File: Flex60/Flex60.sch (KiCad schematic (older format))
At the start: 6 parts

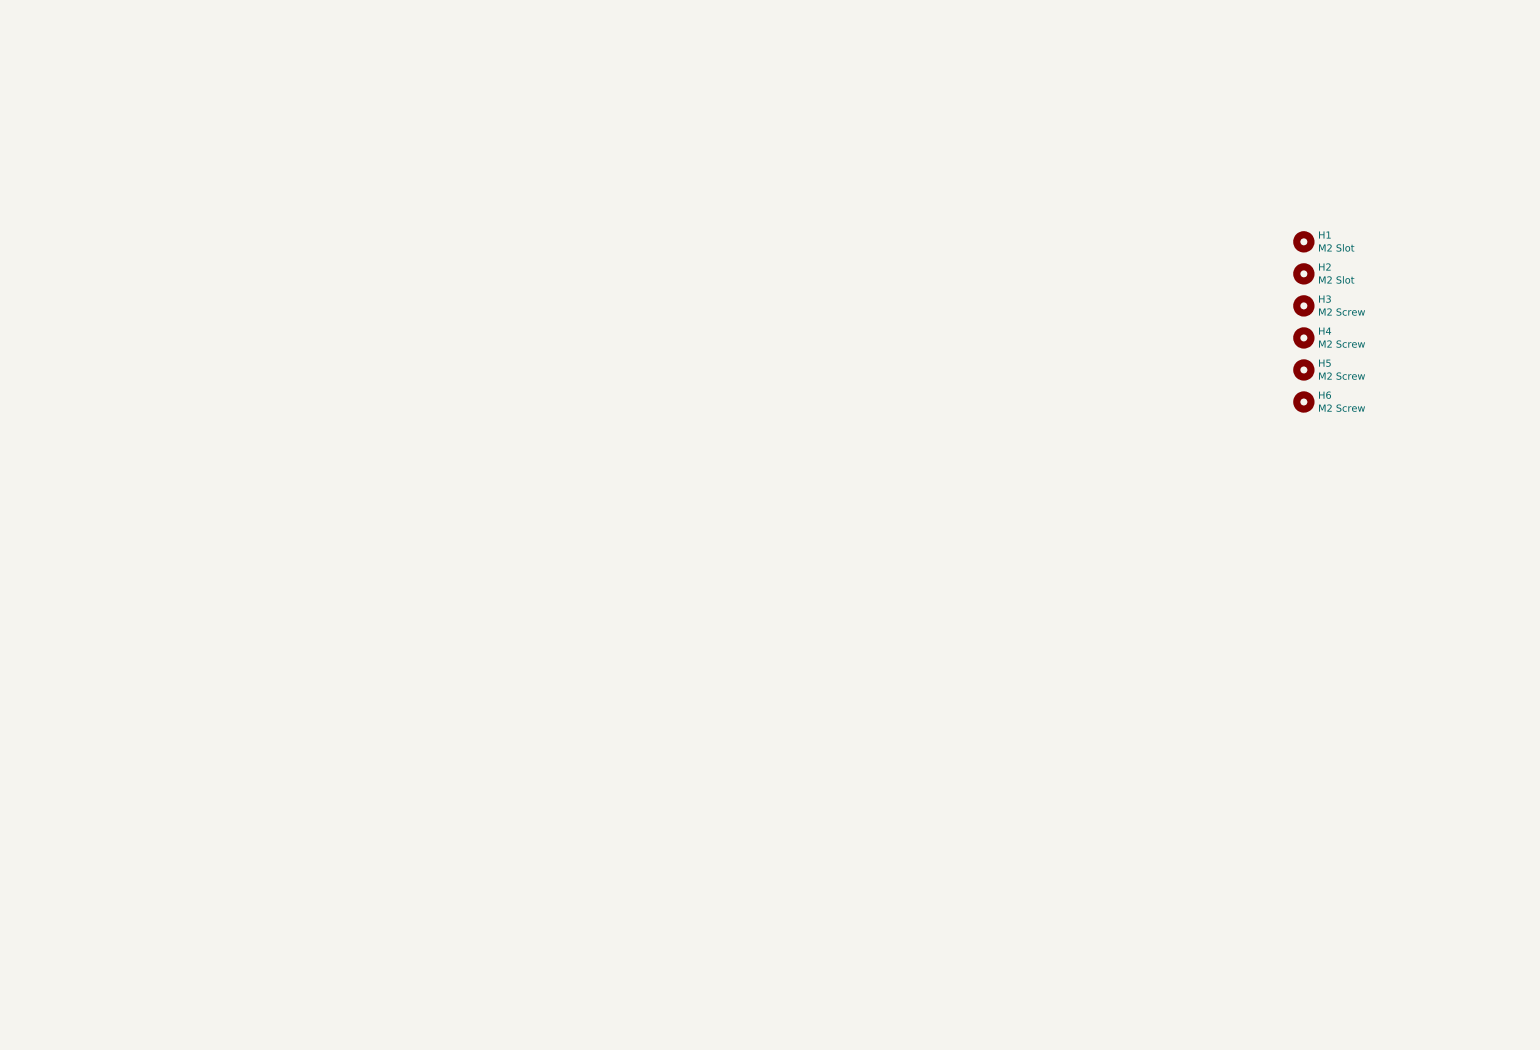
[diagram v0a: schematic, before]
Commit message: Layout of switches
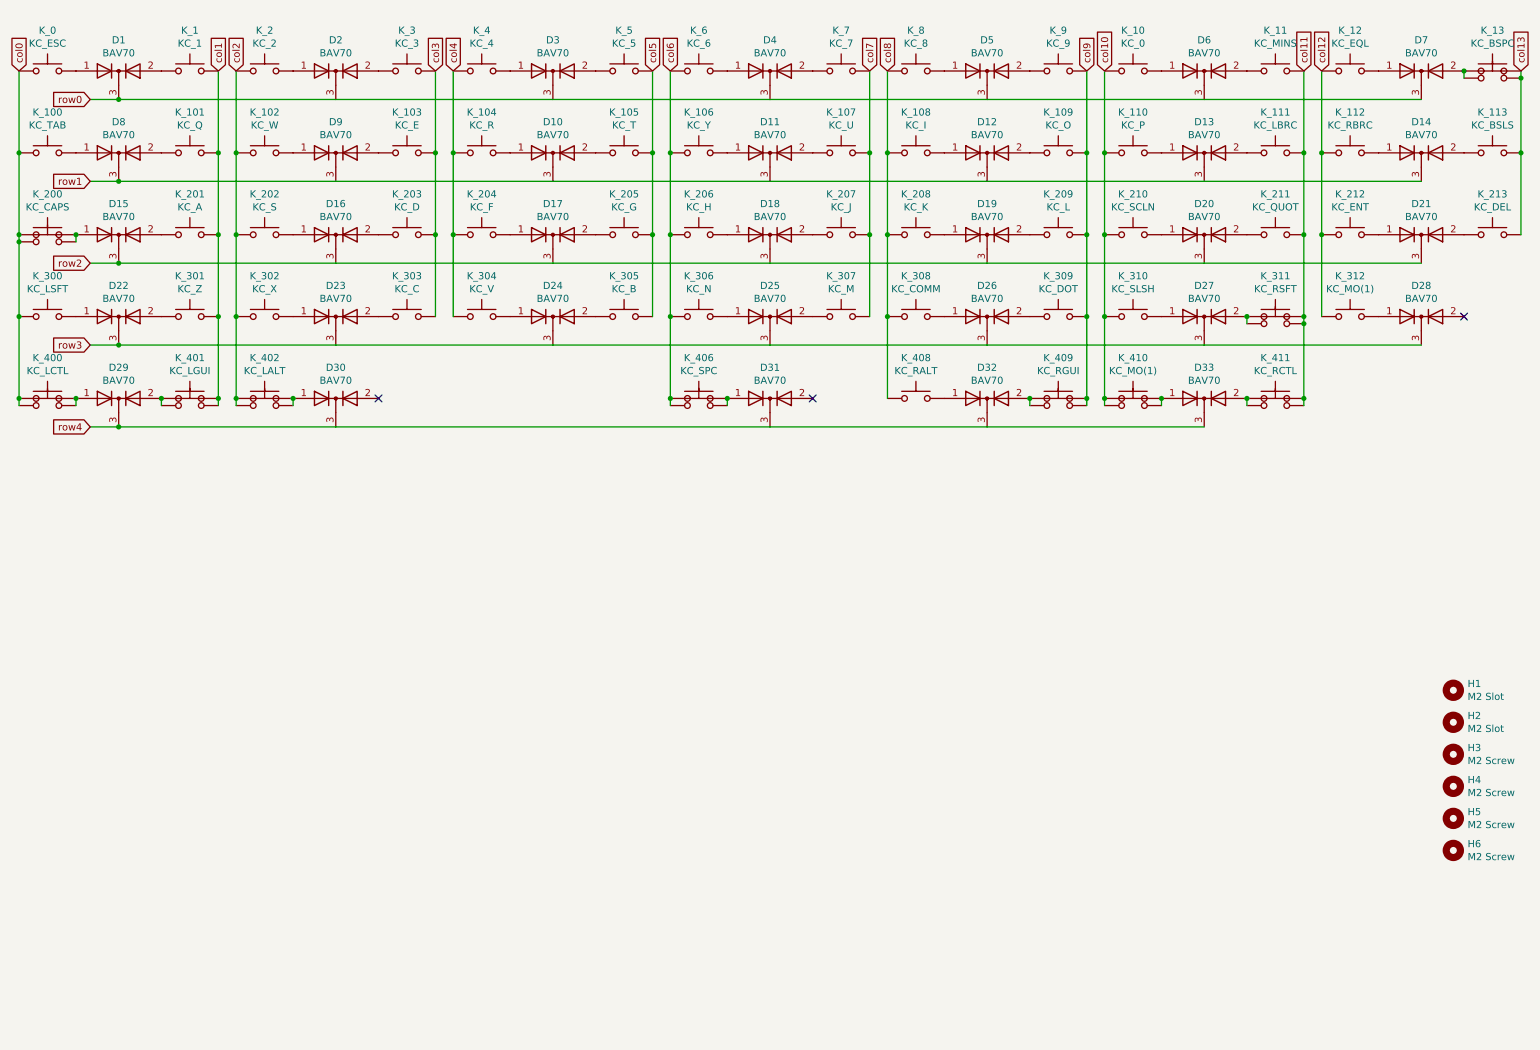
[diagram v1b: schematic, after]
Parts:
- added D1, D10, D11, D12, D13, D14, D15, D16, D17, D18, D19, D2, D20, D21, D22, D23, D24, D25, D26, D27, D28, D29, D3, D30, D31, D32, D33, D4, D5, D6, D7, D8, D9: BAV70, Custom_Footprints:SOT-23_Annotated, symbol Diode:BAV70
- added K_0: KC_ESC, MX_Only:MXOnly-1U-NoLED, symbol Switch:SW_Push
- added K_013A1: KC_BSPC, MX_Only:MXOnly-1U-NoLED, symbol Switch:SW_Push
- added K_1: KC_1, MX_Only:MXOnly-1U-NoLED, symbol Switch:SW_Push
- added K_10: KC_0, MX_Only:MXOnly-1U-NoLED, symbol Switch:SW_Push
- added K_100: KC_TAB, MX_Only:MXOnly-1.5U-NoLED, symbol Switch:SW_Push
- added K_101: KC_Q, MX_Only:MXOnly-1U-NoLED, symbol Switch:SW_Push
- added K_102: KC_W, MX_Only:MXOnly-1U-NoLED, symbol Switch:SW_Push
- added K_103: KC_E, MX_Only:MXOnly-1U-NoLED, symbol Switch:SW_Push
- added K_104: KC_R, MX_Only:MXOnly-1U-NoLED, symbol Switch:SW_Push
- added K_105: KC_T, MX_Only:MXOnly-1U-NoLED, symbol Switch:SW_Push
- added K_106: KC_Y, MX_Only:MXOnly-1U-NoLED, symbol Switch:SW_Push
- added K_107: KC_U, MX_Only:MXOnly-1U-NoLED, symbol Switch:SW_Push
- added K_108: KC_I, MX_Only:MXOnly-1U-NoLED, symbol Switch:SW_Push
- added K_109: KC_O, MX_Only:MXOnly-1U-NoLED, symbol Switch:SW_Push
- added K_11: KC_MINS, MX_Only:MXOnly-1U-NoLED, symbol Switch:SW_Push
- added K_110: KC_P, MX_Only:MXOnly-1U-NoLED, symbol Switch:SW_Push
- added K_111: KC_LBRC, MX_Only:MXOnly-1U-NoLED, symbol Switch:SW_Push
- added K_112: KC_RBRC, MX_Only:MXOnly-1U-NoLED, symbol Switch:SW_Push
- added K_113: KC_BSLS, MX_Only:MXOnly-1.5U-NoLED, symbol Switch:SW_Push
- added K_12: KC_EQL, MX_Only:MXOnly-1U-NoLED, symbol Switch:SW_Push
- added K_13: KC_BSPC, MX_Only:MXOnly-2U-NoLED, symbol Switch:SW_Push
- added K_2: KC_2, MX_Only:MXOnly-1U-NoLED, symbol Switch:SW_Push
- added K_200: KC_CAPS, MX_Only:MXOnly-1.75U-NoLED, symbol Switch:SW_Push
- added K_200A1: KC_CAPS, MX_Only:MXOnly-1.25U-NoLED, symbol Switch:SW_Push
- added K_201: KC_A, MX_Only:MXOnly-1U-NoLED, symbol Switch:SW_Push
- added K_202: KC_S, MX_Only:MXOnly-1U-NoLED, symbol Switch:SW_Push
- added K_203: KC_D, MX_Only:MXOnly-1U-NoLED, symbol Switch:SW_Push
- added K_204: KC_F, MX_Only:MXOnly-1U-NoLED, symbol Switch:SW_Push
- added K_205: KC_G, MX_Only:MXOnly-1U-NoLED, symbol Switch:SW_Push
- added K_206: KC_H, MX_Only:MXOnly-1U-NoLED, symbol Switch:SW_Push
- added K_207: KC_J, MX_Only:MXOnly-1U-NoLED, symbol Switch:SW_Push
- added K_208: KC_K, MX_Only:MXOnly-1U-NoLED, symbol Switch:SW_Push
- added K_209: KC_L, MX_Only:MXOnly-1U-NoLED, symbol Switch:SW_Push
- added K_210: KC_SCLN, MX_Only:MXOnly-1U-NoLED, symbol Switch:SW_Push
- added K_211: KC_QUOT, MX_Only:MXOnly-1U-NoLED, symbol Switch:SW_Push
- added K_212: KC_ENT, MX_Only:MXOnly-2.25U-NoLED, symbol Switch:SW_Push
- added K_213: KC_DEL, MX_Only:MXOnly-1U-NoLED, symbol Switch:SW_Push
- added K_3: KC_3, MX_Only:MXOnly-1U-NoLED, symbol Switch:SW_Push
- added K_300: KC_LSFT, MX_Only:MXOnly-2.25U-NoLED, symbol Switch:SW_Push
- added K_301: KC_Z, MX_Only:MXOnly-1U-NoLED, symbol Switch:SW_Push
- added K_302: KC_X, MX_Only:MXOnly-1U-NoLED, symbol Switch:SW_Push
- added K_303: KC_C, MX_Only:MXOnly-1U-NoLED, symbol Switch:SW_Push
- added K_304: KC_V, MX_Only:MXOnly-1U-NoLED, symbol Switch:SW_Push
- added K_305: KC_B, MX_Only:MXOnly-1U-NoLED, symbol Switch:SW_Push
- added K_306: KC_N, MX_Only:MXOnly-1U-NoLED, symbol Switch:SW_Push
- added K_307: KC_M, MX_Only:MXOnly-1U-NoLED, symbol Switch:SW_Push
- added K_308: KC_COMM, MX_Only:MXOnly-1U-NoLED, symbol Switch:SW_Push
- added K_309: KC_DOT, MX_Only:MXOnly-1U-NoLED, symbol Switch:SW_Push
- added K_310: KC_SLSH, MX_Only:MXOnly-1U-NoLED, symbol Switch:SW_Push
- added K_311: KC_RSFT, MX_Only:MXOnly-2.75U-NoLED, symbol Switch:SW_Push
- added K_311A1: KC_RSFT, MX_Only:MXOnly-1.75U-NoLED, symbol Switch:SW_Push
- added K_312, K_410A1: KC_MO(1), MX_Only:MXOnly-1U-NoLED, symbol Switch:SW_Push
- added K_4: KC_4, MX_Only:MXOnly-1U-NoLED, symbol Switch:SW_Push
- added K_400: KC_LCTL, MX_Only:MXOnly-1.25U-NoLED, symbol Switch:SW_Push
- added K_400A1: KC_LCTL, MX_Only:MXOnly-1.5U-NoLED, symbol Switch:SW_Push
- added K_401: KC_LGUI, MX_Only:MXOnly-1.25U-NoLED, symbol Switch:SW_Push
- added K_401A1: KC_LGUI, MX_Only:MXOnly-1U-NoLED, symbol Switch:SW_Push
- added K_402: KC_LALT, MX_Only:MXOnly-1.25U-NoLED, symbol Switch:SW_Push
- added K_402A1: KC_LALT, MX_Only:MXOnly-1.5U-NoLED, symbol Switch:SW_Push
- added K_406: KC_SPC, MX_Only:MXOnly-6.25U-ReversedStabilizers-NoLED, symbol Switch:SW_Push
- added K_406A1: KC_SPC, MX_Only:MXOnly-7U-ReversedStabilizers-NoLED, symbol Switch:SW_Push
- added K_408: KC_RALT, MX_Only:MXOnly-1.25U-NoLED, symbol Switch:SW_Push
- added K_409: KC_RGUI, MX_Only:MXOnly-1.25U-NoLED, symbol Switch:SW_Push
- added K_409A1: KC_RALT, MX_Only:MXOnly-1.5U-NoLED, symbol Switch:SW_Push
- added K_410: KC_MO(1), MX_Only:MXOnly-1.25U-NoLED, symbol Switch:SW_Push
- added K_411: KC_RCTL, MX_Only:MXOnly-1.25U-NoLED, symbol Switch:SW_Push
- added K_411A1: KC_RCTL, MX_Only:MXOnly-1.5U-NoLED, symbol Switch:SW_Push
- added K_5: KC_5, MX_Only:MXOnly-1U-NoLED, symbol Switch:SW_Push
- added K_6: KC_6, MX_Only:MXOnly-1U-NoLED, symbol Switch:SW_Push
- added K_7: KC_7, MX_Only:MXOnly-1U-NoLED, symbol Switch:SW_Push
- added K_8: KC_8, MX_Only:MXOnly-1U-NoLED, symbol Switch:SW_Push
- added K_9: KC_9, MX_Only:MXOnly-1U-NoLED, symbol Switch:SW_Push
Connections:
- new net: D1.1 (A), K_0.2
- new net: D1.2 (A), K_1.2
- new net: D8.1 (A), K_100.2
- new net: D8.2 (A), K_101.2
- new net: D15.1 (A), K_200.2, K_200A1.2
- new net: D15.2 (A), K_201.2
- new net: D22.1 (A), K_300.2
- new net: D22.2 (A), K_301.2
- new net: D29.1 (A), K_400.2, K_400A1.2
- new net: D29.2 (A), K_401.2, K_401A1.2
- new net: D2.1 (A), K_2.2
- new net: D2.2 (A), K_3.2
- new net: D9.1 (A), K_102.2
- new net: D9.2 (A), K_103.2
- new net: D16.1 (A), K_202.2
- new net: D16.2 (A), K_203.2
- new net: D23.1 (A), K_302.2
- new net: D23.2 (A), K_303.2
- new net: D30.1 (A), K_402.2, K_402A1.2
- new net: D3.1 (A), K_4.2
- new net: D3.2 (A), K_5.2
- new net: D10.1 (A), K_104.2
- new net: D10.2 (A), K_105.2
- new net: D17.1 (A), K_204.2
- new net: D17.2 (A), K_205.2
- new net: D24.1 (A), K_304.2
- new net: D24.2 (A), K_305.2
- new net: D4.1 (A), K_6.2
- new net: D4.2 (A), K_7.2
- new net: D11.1 (A), K_106.2
- new net: D11.2 (A), K_107.2
- new net: D18.1 (A), K_206.2
- new net: D18.2 (A), K_207.2
- new net: D25.1 (A), K_306.2
- new net: D25.2 (A), K_307.2
- new net: D31.1 (A), K_406.2, K_406A1.2
- new net: D5.1 (A), K_8.2
- new net: D5.2 (A), K_9.2
- new net: D12.1 (A), K_108.2
- new net: D12.2 (A), K_109.2
- new net: D19.1 (A), K_208.2
- new net: D19.2 (A), K_209.2
- new net: D26.1 (A), K_308.2
- new net: D26.2 (A), K_309.2
- new net: D32.1 (A), K_408.2
- new net: D32.2 (A), K_409.2, K_409A1.2
- new net: D6.1 (A), K_10.2
- new net: D6.2 (A), K_11.2
- new net: D13.1 (A), K_110.2
- new net: D13.2 (A), K_111.2
- new net: D20.1 (A), K_210.2
- new net: D20.2 (A), K_211.2
- new net: D27.1 (A), K_310.2
- new net: D27.2 (A), K_311.2, K_311A1.2
- new net: D33.1 (A), K_410.2, K_410A1.2
- new net: D33.2 (A), K_411.2, K_411A1.2
- new net: D7.1 (A), K_12.2
- new net: D7.2 (A), K_013A1.2, K_13.2
- new net: D14.1 (A), K_112.2
- new net: D14.2 (A), K_113.2
- new net: D21.1 (A), K_212.2
- new net: D21.2 (A), K_213.2
- new net: D28.1 (A), K_312.2
- new net col0: K_0.1, K_100.1, K_200.1, K_200A1.1, K_300.1, K_400.1, K_400A1.1
- new net col1: K_1.1, K_101.1, K_201.1, K_301.1, K_401.1, K_401A1.1
- new net col10: K_10.1, K_110.1, K_210.1, K_310.1, K_410.1, K_410A1.1
- new net col11: K_11.1, K_111.1, K_211.1, K_311.1, K_311A1.1, K_411.1, K_411A1.1
- new net col12: K_112.1, K_12.1, K_212.1, K_312.1
- new net col13: K_013A1.1, K_113.1, K_13.1, K_213.1
- new net col2: K_102.1, K_2.1, K_202.1, K_302.1, K_402.1, K_402A1.1
- new net col3: K_103.1, K_203.1, K_3.1, K_303.1
- new net col4: K_104.1, K_204.1, K_304.1, K_4.1
- new net col5: K_105.1, K_205.1, K_305.1, K_5.1
- new net col6: K_106.1, K_206.1, K_306.1, K_406.1, K_406A1.1, K_6.1
- new net col7: K_107.1, K_207.1, K_307.1, K_7.1
- new net col8: K_108.1, K_208.1, K_308.1, K_408.1, K_8.1
- new net col9: K_109.1, K_209.1, K_309.1, K_409.1, K_409A1.1, K_9.1
- new net row0: D1.3 (K), D2.3 (K), D3.3 (K), D4.3 (K), D5.3 (K), D6.3 (K), D7.3 (K)
- new net row1: D10.3 (K), D11.3 (K), D12.3 (K), D13.3 (K), D14.3 (K), D8.3 (K), D9.3 (K)
- new net row2: D15.3 (K), D16.3 (K), D17.3 (K), D18.3 (K), D19.3 (K), D20.3 (K), D21.3 (K)
- new net row3: D22.3 (K), D23.3 (K), D24.3 (K), D25.3 (K), D26.3 (K), D27.3 (K), D28.3 (K)
- new net row4: D29.3 (K), D30.3 (K), D31.3 (K), D32.3 (K), D33.3 (K)
- no-connect marks 0 -> 3
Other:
- moved on the sheet: H1, H2, H3, H4, H5, H6
